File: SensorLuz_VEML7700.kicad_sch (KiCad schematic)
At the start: 6 parts, among them U10 Green LED

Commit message: PCB ordenada V1
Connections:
- net I2C2_SCL renamed I2C1_SCL
- net I2C2_SDA renamed I2C1_SDA
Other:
- moved on the sheet: C31, C32, R9
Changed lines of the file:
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@@
 	(paper "A4")
 	(junction
-		(at 91.44 81.28)
+		(at 137.16 39.37)
 		(diameter 0)
 		(color 0 0 0 0)
 	)
 	(junction
-		(at 74.93 81.28)
+		(at 120.65 39.37)
 		(diameter 0)
 		(color 0 0 0 0)
@@
 	(wire
 		(pts
-			(xy 91.44 96.52) (xy 91.44 99.06)
+			(xy 137.16 54.61) (xy 137.16 57.15)
 		)
 		(stroke
@@
 	(wire
 		(pts
-			(xy 74.93 81.28) (xy 74.93 86.36)
+			(xy 120.65 39.37) (xy 120.65 44.45)
 		)
 		(stroke
@@
 	(wire
 		(pts
-			(xy 91.44 81.28) (xy 91.44 86.36)
+			(xy 137.16 39.37) (xy 137.16 44.45)
 		)
 		(stroke
@@
 	(wire
 		(pts
-			(xy 123.19 76.2) (xy 123.19 78.74)
+			(xy 120.65 54.61) (xy 120.65 57.15)
 		)
 		(stroke
@@
 	(wire
 		(pts
-			(xy 74.93 96.52) (xy 74.93 99.06)
+			(xy 137.16 39.37) (xy 142.24 39.37)
 		)
 		(stroke
@@
 	(wire
 		(pts
-			(xy 91.44 81.28) (xy 96.52 81.28)
+			(xy 90.17 39.37) (xy 102.87 39.37)
 		)
 		(stroke
@@
 	(wire
 		(pts
-			(xy 44.45 81.28) (xy 57.15 81.28)
+			(xy 167.64 88.9) (xy 167.64 91.44)
 		)
 		(stroke
@@
 	(wire
 		(pts
-			(xy 167.64 88.9) (xy 167.64 91.44)
+			(xy 167.64 72.39) (xy 167.64 78.74)
 		)
 		(stroke
@@
 	(wire
 		(pts
-			(xy 167.64 72.39) (xy 167.64 78.74)
+			(xy 90.17 30.48) (xy 90.17 39.37)
 		)
 		(stroke
@@
 	(wire
 		(pts
-			(xy 44.45 72.39) (xy 44.45 81.28)
+			(xy 167.64 101.6) (xy 167.64 104.14)
 		)
 		(stroke
@@
 	(wire
 		(pts
-			(xy 167.64 101.6) (xy 167.64 104.14)
+			(xy 111.76 83.82) (xy 123.19 83.82)
 		)
 		(stroke
@@
 	(wire
 		(pts
-			(xy 111.76 83.82) (xy 123.19 83.82)
+			(xy 120.65 39.37) (xy 137.16 39.37)
 		)
 		(stroke
@@
 	(wire
 		(pts
-			(xy 74.93 81.28) (xy 91.44 81.28)
+			(xy 102.87 81.28) (xy 123.19 81.28)
 		)
 		(stroke
@@
 	(wire
 		(pts
-			(xy 113.03 81.28) (xy 123.19 81.28)
-		)
-		(stroke
-			(width 0)
-			(type default)
-		)
-	)
-	(wire
-		(pts
-			(xy 64.77 81.28) (xy 74.93 81.28)
+			(xy 110.49 39.37) (xy 120.65 39.37)
 		)
 		(stroke
@@
 	)
 	(label "VDD_LUZ"
-		(at 96.52 81.28 0)
+		(at 142.24 39.37 0)
 		(effects
 			(font
@@
 	)
 	(label "VDD_LUZ"
-		(at 113.03 81.28 0)
+		(at 102.87 81.28 0)
 		(effects
 			(font
@@
 		)
 	)
-	(global_label "I2C2_SDA"
+	(global_label "I2C1_SDA"
 		(shape input)
 		(at 123.19 86.36 180)
@@
 		)
 	)
-	(global_label "I2C2_SCL"
+	(global_label "I2C1_SCL"
 		(shape input)
-		(at 123.19 76.2 180)
+		(at 123.19 78.74 180)
 		(fields_autoplaced yes)
 		(effects
@@
 		)
 		(property "Intersheetrefs" "${INTERSHEET_REFS}"
-			(at 111.4358 76.2 0)
+			(at 111.4358 78.74 0)
 			(hide yes)
 			(show_name no)
@@
 	(symbol
 		(lib_id "power:GND")
-		(at 91.44 99.06 0)
+		(at 137.16 57.15 0)
 		(unit 1)
 		(body_style 1)
@@
 		(fields_autoplaced yes)
 		(property "Reference" "#PWR074"
-			(at 91.44 105.41 0)
+			(at 137.16 63.5 0)
 			(hide yes)
 			(show_name no)
@@
 		)
 		(property "Value" "GND"
-			(at 91.44 104.14 0)
+			(at 137.16 62.23 0)
 			(show_name no)
 			(do_not_autoplace no)
@@
 		)
 		(property "Footprint" ""
-			(at 91.44 99.06 0)
+			(at 137.16 57.15 0)
 			(hide yes)
 			(show_name no)
@@
 		)
 		(property "Datasheet" ""
-			(at 91.44 99.06 0)
+			(at 137.16 57.15 0)
 			(hide yes)
 			(show_name no)
@@
 		)
 		(property "Description" "Power symbol creates a global label with name \"GND\" , ground"
-			(at 91.44 99.06 0)
+			(at 137.16 57.15 0)
 			(hide yes)
 			(show_name no)
@@
 	(symbol
 		(lib_id "CANSAT_STM32_symbols:TCC0402X7R104J500AT")
-		(at 74.93 91.44 90)
+		(at 120.65 49.53 90)
 		(unit 1)
 		(body_style 1)
@@
 		(fields_autoplaced yes)
 		(property "Reference" "C31"
-			(at 78.74 90.1699 90)
+			(at 124.46 48.2599 90)
 			(show_name no)
 			(do_not_autoplace no)
@@
 		)
 		(property "Value" "100nF"
-			(at 78.74 92.7099 90)
+			(at 124.46 50.7999 90)
 			(show_name no)
 			(do_not_autoplace no)
@@
 		)
 		(property "Footprint" "ARLISS-footprints:C0402"
-			(at 82.55 91.44 0)
+			(at 128.27 49.53 0)
 			(hide yes)
 			(show_name no)
@@
 		)
 		(property "Datasheet" "https://www.lcsc.com/datasheet/C5448844.pdf"
-			(at 85.09 91.44 0)
+			(at 130.81 49.53 0)
 			(hide yes)
 			(show_name no)
@@
 		)
 		(property "Description" ""
-			(at 74.93 91.44 0)
+			(at 120.65 49.53 0)
 			(hide yes)
 			(show_name no)
@@
 		)
 		(property "Manufacturer" "CCTC(三环)"
-			(at 87.63 91.44 0)
+			(at 133.35 49.53 0)
 			(hide yes)
 			(show_name no)
@@
 		)
 		(property "MPN" "TCC0402X7R104J500AT"
-			(at 90.17 91.44 0)
+			(at 135.89 49.53 0)
 			(hide yes)
 			(show_name no)
@@
 		)
 		(property "LCSC Part" "C5448844"
-			(at 92.71 91.44 0)
+			(at 138.43 49.53 0)
 			(hide yes)
 			(show_name no)
@@
 	(symbol
 		(lib_id "Device:R")
-		(at 60.96 81.28 90)
+		(at 106.68 39.37 90)
 		(unit 1)
 		(body_style 1)
@@
 		(fields_autoplaced yes)
 		(property "Reference" "R9"
-			(at 60.96 74.93 90)
+			(at 106.68 33.02 90)
 			(show_name no)
 			(do_not_autoplace no)
@@
 		)
 		(property "Value" "10"
-			(at 60.96 77.47 90)
+			(at 106.68 35.56 90)
 			(show_name no)
 			(do_not_autoplace no)
@@
 		)
 		(property "Footprint" "Resistor_SMD:R_0402_1005Metric_Pad0.72x0.64mm_HandSolder"
-			(at 60.96 83.058 90)
+			(at 106.68 41.148 90)
 			(hide yes)
 			(show_name no)
@@
 		)
 		(property "Datasheet" ""
-			(at 60.96 81.28 0)
+			(at 106.68 39.37 0)
 			(hide yes)
 			(show_name no)
@@
 		)
 		(property "Description" "Resistor"
-			(at 60.96 81.28 0)
+			(at 106.68 39.37 0)
 			(hide yes)
 			(show_name no)
@@
 		)
 		(property "LCSC" "C854481"
-			(at 60.96 81.28 90)
+			(at 106.68 39.37 90)
 			(hide yes)
 			(show_name no)
@@
 	(symbol
 		(lib_id "CANSAT_STM32_symbols:UUA1H100MCL1GS")
-		(at 91.44 91.44 270)
+		(at 137.16 49.53 270)
 		(unit 1)
 		(body_style 1)
@@
 		(fields_autoplaced yes)
 		(property "Reference" "C32"
-			(at 93.98 90.1699 90)
+			(at 139.7 48.2599 90)
 			(show_name no)
 			(do_not_autoplace no)
@@
 		)
 		(property "Value" "10uF"
-			(at 93.98 92.7099 90)
+			(at 139.7 50.7999 90)
 			(show_name no)
 			(do_not_autoplace no)
@@
 		)
 		(property "Footprint" "ARLISS-footprints:CAP-SMD_BD6.3-L6.6-W6.6-LS7.3"
-			(at 83.82 91.44 0)
+			(at 129.54 49.53 0)
 			(hide yes)
 			(show_name no)
@@
 		)
 		(property "Datasheet" "https://www.lcsc.com/datasheet/C2163451.pdf"
-			(at 81.28 91.44 0)
+			(at 127 49.53 0)
 			(hide yes)
 			(show_name no)
@@
 		)
 		(property "Description" ""
-			(at 91.44 91.44 0)
+			(at 137.16 49.53 0)
 			(hide yes)
 			(show_name no)
@@
 		)
 		(property "Manufacturer" "Nichicon(尼吉康)"
-			(at 78.74 91.44 0)
+			(at 124.46 49.53 0)
 			(hide yes)
 			(show_name no)
@@
 		)
 		(property "MPN" "UUA1H100MCL1GS"
-			(at 76.2 91.44 0)
+			(at 121.92 49.53 0)
 			(hide yes)
 			(show_name no)
@@
 		)
 		(property "LCSC Part" "C2163451"
-			(at 73.66 91.44 0)
+			(at 119.38 49.53 0)
 			(hide yes)
 			(show_name no)
@@
 		(instances
 			(project "ARLISS_STM32_2026"
+				(path "/9719ea46-14c4-4409-9c57-49dd5454c03f/55efcca8-1297-47b0-ad35-b3f1b6f19299"
+					(reference "C32")
+					(unit 1)
+				)
 				(path "/9719ea46-14c4-4409-9c57-49dd5454c03f/90e9a371-b783-4b2a-a8c2-544713e1ebd2"
 					(reference "C32")
@@
 	(symbol
 		(lib_id "power:+3V3")
-		(at 44.45 72.39 0)
+		(at 90.17 30.48 0)
 		(unit 1)
 		(body_style 1)
@@
 		(fields_autoplaced yes)
 		(property "Reference" "#PWR068"
-			(at 44.45 76.2 0)
+			(at 90.17 34.29 0)
 			(hide yes)
 			(show_name no)
@@
 		)
 		(property "Value" "+3V3"
-			(at 44.45 67.31 0)
+			(at 90.17 25.4 0)
 			(show_name no)
 			(do_not_autoplace no)
@@
 		)
 		(property "Footprint" ""
-			(at 44.45 72.39 0)
+			(at 90.17 30.48 0)
 			(hide yes)
 			(show_name no)
@@
 		)
 		(property "Datasheet" ""
-			(at 44.45 72.39 0)
+			(at 90.17 30.48 0)
 			(hide yes)
 			(show_name no)
@@
 		)
 		(property "Description" "Power symbol creates a global label with name \"+3V3\""
-			(at 44.45 72.39 0)
+			(at 90.17 30.48 0)
 			(hide yes)
 			(show_name no)
@@
 	(symbol
 		(lib_id "power:GND")
-		(at 74.93 99.06 0)
+		(at 120.65 57.15 0)
 		(unit 1)
 		(body_style 1)
@@
 		(fields_autoplaced yes)
 		(property "Reference" "#PWR073"
-			(at 74.93 105.41 0)
+			(at 120.65 63.5 0)
 			(hide yes)
 			(show_name no)
@@
 		)
 		(property "Value" "GND"
-			(at 74.93 104.14 0)
+			(at 120.65 62.23 0)
 			(show_name no)
 			(do_not_autoplace no)
@@
 		)
 		(property "Footprint" ""
-			(at 74.93 99.06 0)
+			(at 120.65 57.15 0)
 			(hide yes)
 			(show_name no)
@@
 		)
 		(property "Datasheet" ""
-			(at 74.93 99.06 0)
+			(at 120.65 57.15 0)
 			(hide yes)
 			(show_name no)
@@
 		)
 		(property "Description" "Power symbol creates a global label with name \"GND\" , ground"
-			(at 74.93 99.06 0)
-			(hide yes)
-			(show_name no)
+			(at 120.65 57.15 0)
+			(hide yes)
+			(show_name no)

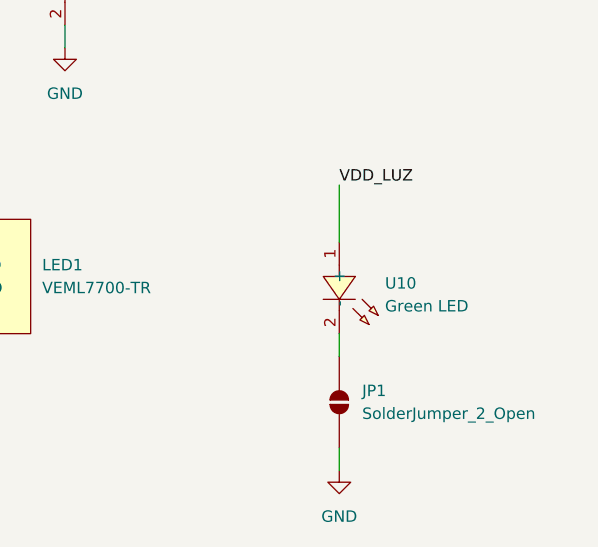
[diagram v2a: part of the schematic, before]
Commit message: Primer Ruteo de PCB
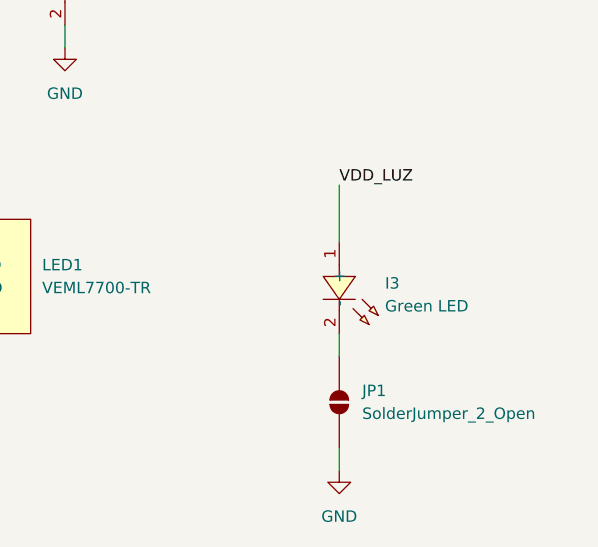
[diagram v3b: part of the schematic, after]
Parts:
- C31: footprint ARLISS-footprints:C0402 -> Capacitor_SMD:C_0402_1005Metric_Pad0.74x0.62mm_HandSolder
- renumbered U10 to I3
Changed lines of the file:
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@@
 			)
 		)
-		(property "Footprint" "ARLISS-footprints:C0402"
+		(property "Footprint" "Capacitor_SMD:C_0402_1005Metric_Pad0.74x0.62mm_HandSolder"
 			(at 128.27 49.53 0)
 			(hide yes)
@@
 		(dnp no)
 		(fields_autoplaced yes)
-		(property "Reference" "U10"
+		(property "Reference" "I3"
 			(at 172.72 83.3099 90)
 			(show_name no)
@@
 			(project "ARLISS_STM32_2026"
 				(path "/9719ea46-14c4-4409-9c57-49dd5454c03f/90e9a371-b783-4b2a-a8c2-544713e1ebd2"
-					(reference "U10")
+					(reference "I3")
 					(unit 1)
 				)

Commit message: Arreglos de esquemático
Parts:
- removed I3: Green LED, ARLISS-footprints:LED0603-FD, symbol CANSAT_STM32_symbols:YLED0603G
- removed JP1: SolderJumper_2_Open, Jumper:SolderJumper-2_P1.3mm_Open_TrianglePad1.0x1.5mm, symbol Jumper:SolderJumper_2_Open
- R9: footprint Resistor_SMD:R_0402_1005Metric_Pad0.72x0.64mm_HandSolder -> Resistor_SMD:R_0603_1608Metric_Pad0.98x0.95mm_HandSolder; LCSC C854481 -> (none); LCSC part (none) -> https://www.lcsc.com/product-detail/C163851.html?s_z=n_q_t_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
- renumbered LED1 to U9

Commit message: Arreglando footprints
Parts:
- C29: renamed from C31; footprint Capacitor_SMD:C_0402_1005Metric_Pad0.74x0.62mm_HandSolder -> Capacitor_SMD:C_0603_1608Metric_Pad1.08x0.95mm_HandSolder; Manufacturer CCTC(三环) -> (none)
- C30: renamed from C32; Manufacturer Nichicon(尼吉康) -> (none)
- R12: renamed from R9; LCSC part https://www.lcsc.com/product-detail/C163851.html?s_z=n_q_t_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 -> (none)
- U6: renamed from U9; Manufacturer VISHAY(威世) -> (none)
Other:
- company: (none) -> TOMEK TEAM
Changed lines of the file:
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@@
 	(generator_version "10.0")
 	(paper "A4")
+	(title_block
+		(company "TOMEK TEAM")
+	)
 	(junction
 		(at 137.16 39.37)
@@
 		(dnp no)
 		(fields_autoplaced yes)
-		(property "Reference" "R9"
+		(property "Reference" "R12"
 			(at 106.68 33.02 90)
 			(show_name no)
@@
 		(property "Description" "Resistor"
 			(at 106.68 39.37 0)
-			(hide yes)
-			(show_name no)
-			(do_not_autoplace no)
-			(effects
-				(font
-					(size 1.27 1.27)
-				)
-			)
-		)
-		(property "LCSC part" "https://www.lcsc.com/product-detail/C163851.html?s_z=n_q_t_resistor&spm=wm.fly.bg.0.xh___wm.ssy.tc.0.tz&lcsc_vid=E1ILBlYFElddBQdfFFddA1cCFVMPAwJUFFEMVwAFEgAxVlNeRVFeX1NWRFFWUjsOAxUeFF5JWBYZEEoKFBINSQcJGk4%3D"
-			(at 106.68 39.37 90)
 			(hide yes)
 			(show_name no)
@@
 			(project "ARLISS_STM32_2026"
 				(path "/9719ea46-14c4-4409-9c57-49dd5454c03f/90e9a371-b783-4b2a-a8c2-544713e1ebd2"
-					(reference "R9")
+					(reference "R12")
 					(unit 1)
 				)
@@
 		(dnp no)
 		(fields_autoplaced yes)
-		(property "Reference" "#PWR074"
+		(property "Reference" "#PWR073"
 			(at 137.16 63.5 0)
 			(hide yes)
@@
 			(project "ARLISS_STM32_2026"
 				(path "/9719ea46-14c4-4409-9c57-49dd5454c03f/90e9a371-b783-4b2a-a8c2-544713e1ebd2"
-					(reference "#PWR074")
+					(reference "#PWR073")
 					(unit 1)
 				)
@@
 		(dnp no)
 		(fields_autoplaced yes)
-		(property "Reference" "C31"
+		(property "Reference" "C29"
 			(at 124.46 48.2599 90)
 			(show_name no)
@@
 			)
 		)
-		(property "Footprint" "Capacitor_SMD:C_0402_1005Metric_Pad0.74x0.62mm_HandSolder"
+		(property "Footprint" "Capacitor_SMD:C_0603_1608Metric_Pad1.08x0.95mm_HandSolder"
 			(at 128.27 49.53 0)
 			(hide yes)
@@
 		(property "Description" ""
 			(at 120.65 49.53 0)
-			(hide yes)
-			(show_name no)
-			(do_not_autoplace no)
-			(effects
-				(font
-					(size 1.27 1.27)
-				)
-			)
-		)
-		(property "Manufacturer" "CCTC(三环)"
-			(at 133.35 49.53 0)
 			(hide yes)
 			(show_name no)
@@
 			(project "ARLISS_STM32_2026"
 				(path "/9719ea46-14c4-4409-9c57-49dd5454c03f/90e9a371-b783-4b2a-a8c2-544713e1ebd2"
-					(reference "C31")
+					(reference "C29")
 					(unit 1)
 				)
@@
 		(dnp no)
 		(fields_autoplaced yes)
-		(property "Reference" "#PWR072"
+		(property "Reference" "#PWR071"
 			(at 105.41 83.82 0)
 			(hide yes)
@@
 			(project "ARLISS_STM32_2026"
 				(path "/9719ea46-14c4-4409-9c57-49dd5454c03f/90e9a371-b783-4b2a-a8c2-544713e1ebd2"
-					(reference "#PWR072")
+					(reference "#PWR071")
 					(unit 1)
 				)
@@
 		(dnp no)
 		(fields_autoplaced yes)
-		(property "Reference" "U9"
+		(property "Reference" "U6"
 			(at 134.62 81.2799 0)
 			(show_name no)
@@
 		(property "Description" ""
 			(at 128.27 82.55 0)
-			(hide yes)
-			(show_name no)
-			(do_not_autoplace no)
-			(effects
-				(font
-					(size 1.27 1.27)
-				)
-			)
-		)
-		(property "Manufacturer" "VISHAY(威世)"
-			(at 128.27 99.06 0)
 			(hide yes)
 			(show_name no)
@@
 			(project "ARLISS_STM32_2026"
 				(path "/9719ea46-14c4-4409-9c57-49dd5454c03f/90e9a371-b783-4b2a-a8c2-544713e1ebd2"
-					(reference "U9")
+					(reference "U6")
 					(unit 1)
 				)
@@
 		(dnp no)
 		(fields_autoplaced yes)
-		(property "Reference" "C32"
+		(property "Reference" "C30"
 			(at 139.7 48.2599 90)
 			(show_name no)
@@
 		(property "Description" ""
 			(at 137.16 49.53 0)
-			(hide yes)
-			(show_name no)
-			(do_not_autoplace no)
-			(effects
-				(font
-					(size 1.27 1.27)
-				)
-			)
-		)
-		(property "Manufacturer" "Nichicon(尼吉康)"
-			(at 124.46 49.53 0)
 			(hide yes)
 			(show_name no)
@@
 			(project "ARLISS_STM32_2026"
 				(path "/9719ea46-14c4-4409-9c57-49dd5454c03f/90e9a371-b783-4b2a-a8c2-544713e1ebd2"
-					(reference "C32")
+					(reference "C30")
 					(unit 1)
 				)
@@
 		(dnp no)
 		(fields_autoplaced yes)
-		(property "Reference" "#PWR068"
+		(property "Reference" "#PWR070"
 			(at 90.17 34.29 0)
 			(hide yes)
@@
 			(project "ARLISS_STM32_2026"
 				(path "/9719ea46-14c4-4409-9c57-49dd5454c03f/90e9a371-b783-4b2a-a8c2-544713e1ebd2"
-					(reference "#PWR068")
+					(reference "#PWR070")
 					(unit 1)
 				)
@@
 		(dnp no)
 		(fields_autoplaced yes)
-		(property "Reference" "#PWR073"
+		(property "Reference" "#PWR072"
 			(at 120.65 63.5 0)
 			(hide yes)
@@
 			(project "ARLISS_STM32_2026"
 				(path "/9719ea46-14c4-4409-9c57-49dd5454c03f/90e9a371-b783-4b2a-a8c2-544713e1ebd2"
-					(reference "#PWR073")
+					(reference "#PWR072")
 					(unit 1)
 				)
